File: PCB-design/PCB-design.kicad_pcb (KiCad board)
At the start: 2 copper layers, 1 part

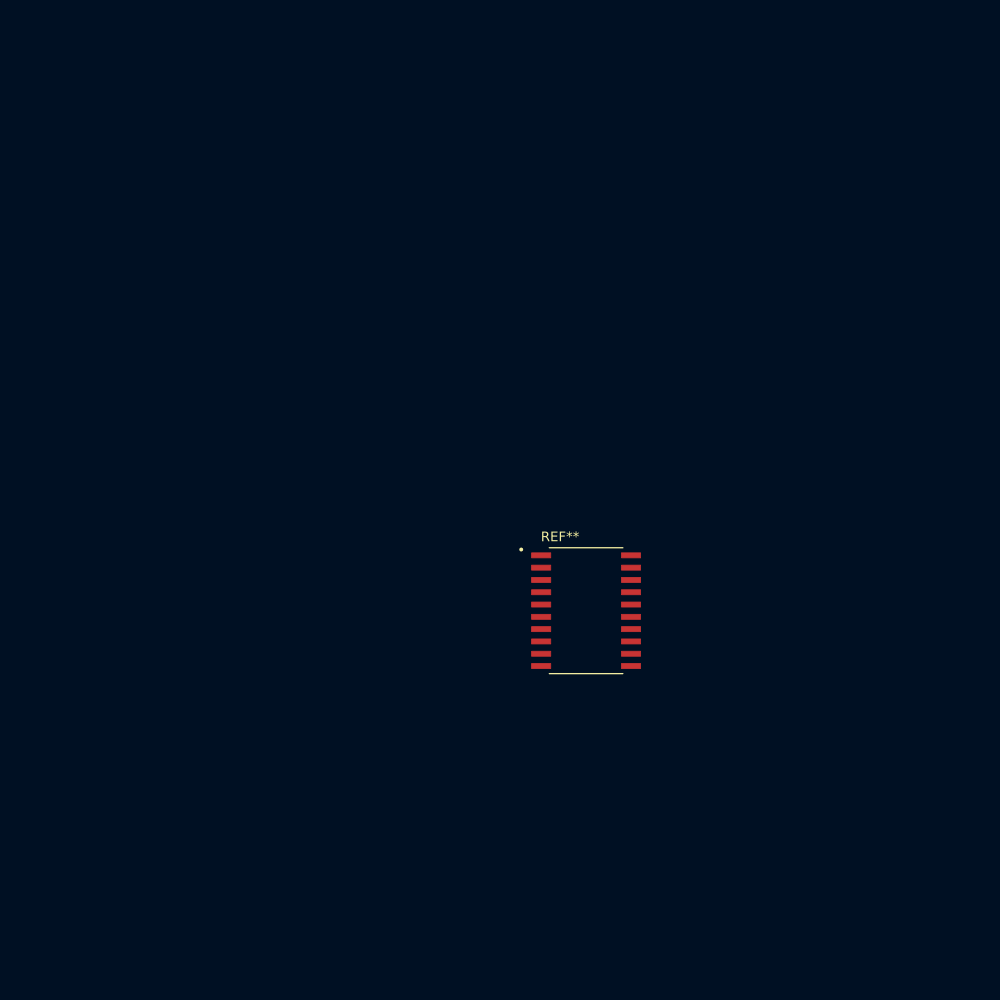
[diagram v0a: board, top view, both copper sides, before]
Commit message: connections to APFC IC
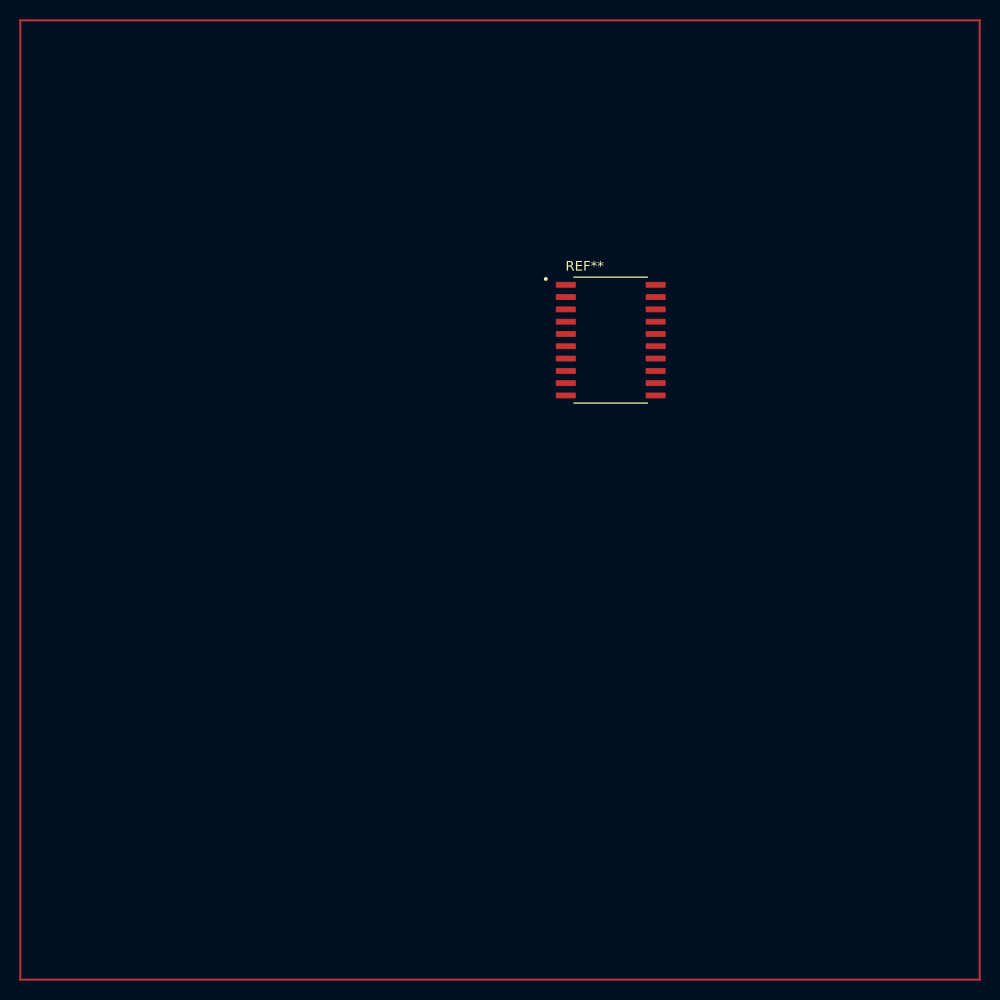
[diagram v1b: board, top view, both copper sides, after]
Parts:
- moved REF** 28.1 mm to (157.5, 71.1)
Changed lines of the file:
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@@
   (net 0 "")
   (footprint "UCC28070:SOIC127P1030X265-20N" (layer "F.Cu")
-    (at 154.94 99.06)
+    (at 157.48 71.12)
     (attr smd)
     (fp_text reference "REF**" (at -2.685 -7.635) (layer "F.SilkS")
@@
       (solder_mask_margin 0.102))
   )
+  (gr_line (start 195.58 38.1) (end 96.52 38.1)
+    (stroke (width 0.2) (type default)) (layer "F.Cu"))
+  (gr_line (start 96.52 137.16) (end 195.58 137.16)
+    (stroke (width 0.2) (type default)) (layer "F.Cu"))
+  (gr_line (start 96.52 38.1) (end 96.52 137.16)
+    (stroke (width 0.2) (type default)) (layer "F.Cu"))
+  (gr_line (start 195.58 137.16) (end 195.58 38.1)
+    (stroke (width 0.2) (type default)) (layer "F.Cu"))
 )
